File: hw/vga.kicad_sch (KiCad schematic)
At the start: 19 parts, among them J1 Conn_02x05_Odd_Even, J2 DB15_Female_HighDensity_Mount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, U1 74HC4053, U2 23LCV512, U3 ICS501

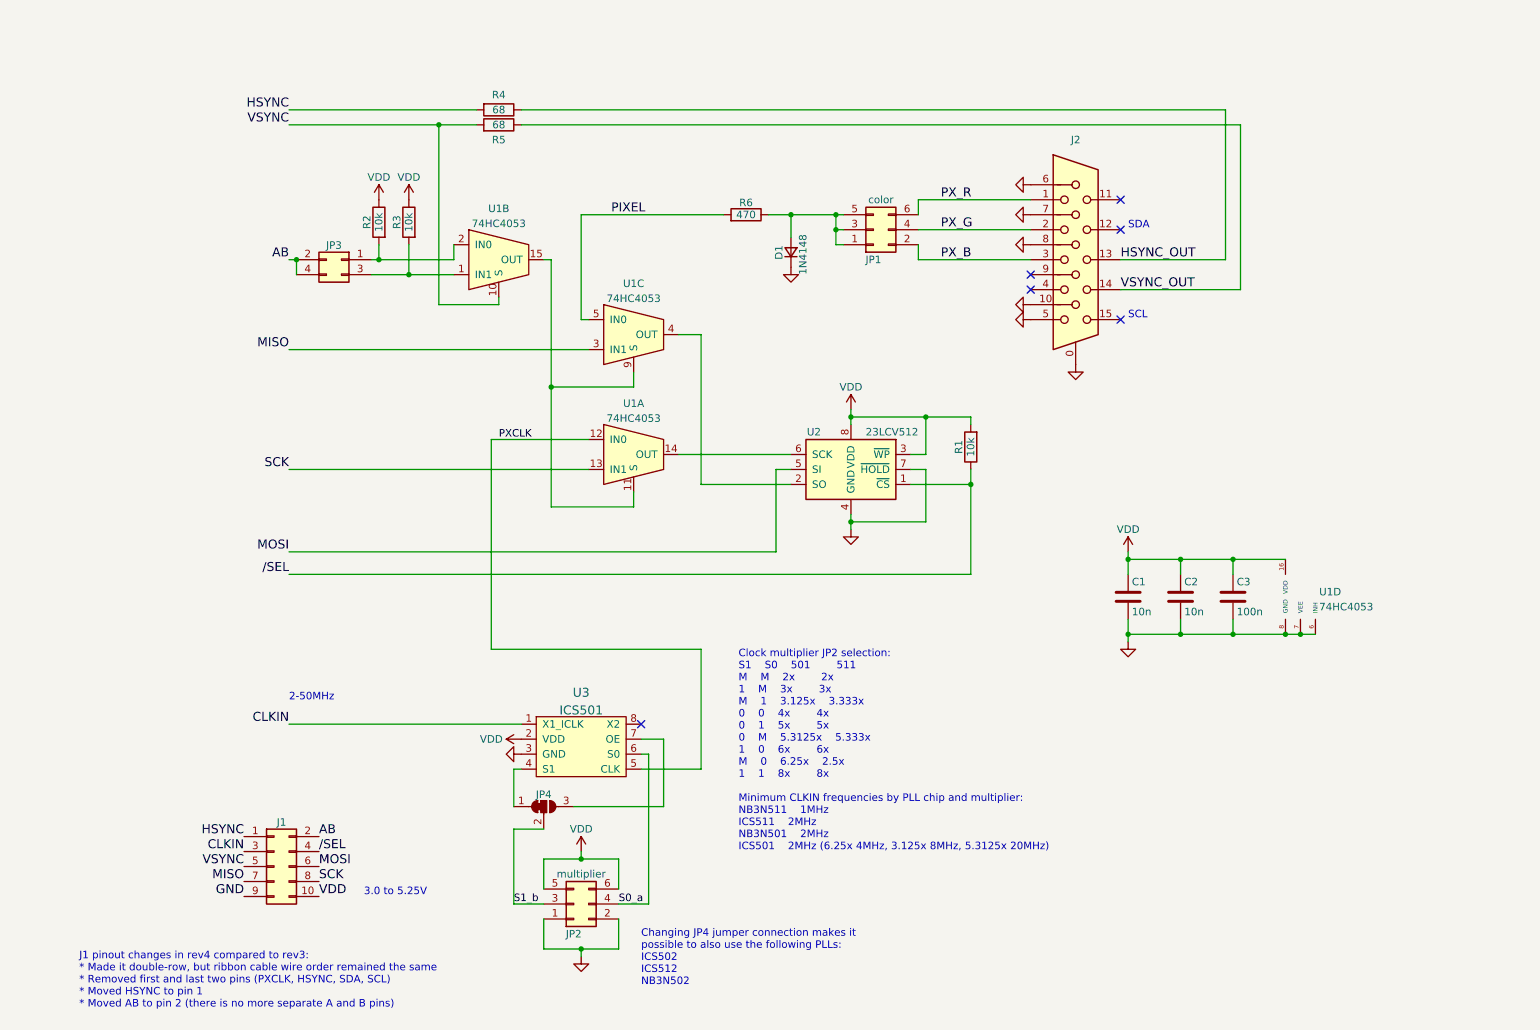
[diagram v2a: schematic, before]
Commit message: Finalized rev4 board. Added post PCB manufacturing TODOs to schematic.
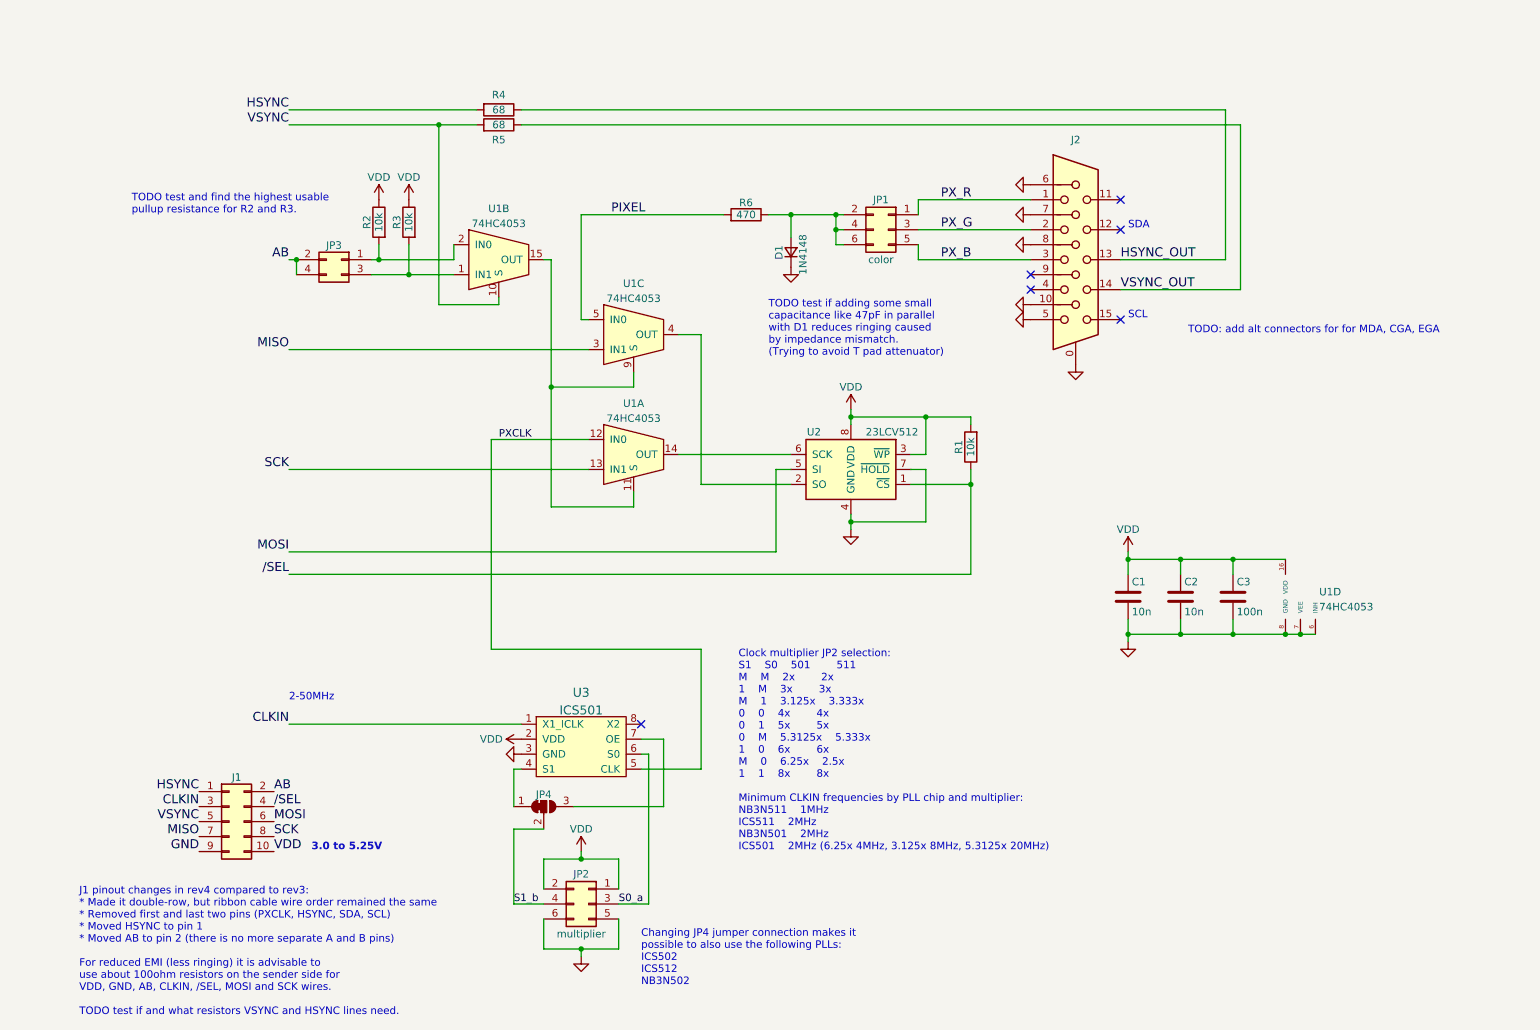
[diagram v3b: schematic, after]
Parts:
- D1: footprint Diode_SMD:D_SOD-323_HandSoldering -> Diode_SMD:D_SOD-123
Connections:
- net GND: now also JP2.5 (Pin_5), JP2.6 (Pin_6); no longer JP2.1 (Pin_1), JP2.2 (Pin_2)
- net PX_B: now also JP1.5 (Pin_5); no longer JP1.2 (Pin_2)
- net PX_G: now also JP1.3 (Pin_3); no longer JP1.4 (Pin_4)
- net PX_R: now also JP1.1 (Pin_1); no longer JP1.6 (Pin_6)
- net S0_a: now also JP2.3 (Pin_3); no longer JP2.4 (Pin_4)
- net S1_b: now also JP2.4 (Pin_4); no longer JP2.3 (Pin_3)
- net VDD: now also JP2.1 (Pin_1), JP2.2 (Pin_2); no longer JP2.5 (Pin_5), JP2.6 (Pin_6)
- new net: D1.2 (A), JP1.2 (Pin_2), JP1.4 (Pin_4), JP1.6 (Pin_6), R6.1
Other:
- note added: "J1 pinout changes in rev4 compared to rev3: * Made it double-row, but ribbon cable wire order remained the same * Removed first and last two pins (PXCLK, HSYNC, SDA, SCL) * Moved HSYNC to pin 1 * Moved AB to pin 2 (there is no more separate A and B pins) For reduced EMI (less ringing) it is advisable to use about 100ohm resistors on the sender side for VDD, GND, AB, CLKIN, /SEL, MOSI and SCK wire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"
- note added: "TODO test and find the highest usable pullup resistance for R2 and R3."
- note added: "TODO test if adding some small capacitance like 47pF in parallel with D1 reduces ringing caused by impedance mismatch. (Trying to avoid T pad attenuator)"
- note added: "TODO: add alt connectors for for MDA, CGA, EGA"
- note removed: "J1 pinout changes in rev4 compared to rev3: * Made it double-row, but ribbon cable wire order remained the same * Removed first and last two pins (PXCLK, HSYNC, SDA, SCL) * Moved HSYNC to pin 1 * Moved AB to pin 2 (there is no more separate A and B pins)"
- moved on the sheet: J1
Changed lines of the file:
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@@
+    (effects (font (size 1.27 1.27)) (justify left bottom))
+  )
+  (text "TODO: add alt connectors for for MDA, CGA, EGA" (at 217.17 76.2 0)
     (effects (font (size 1.27 1.27)) (justify left bottom))
   )
@@
     (effects (font (size 1.27 1.27)) (justify left bottom))
   )
-  (text "J1 pinout changes in rev4 compared to rev3:\n* Made it double-row, but ribbon cable wire order remained the same\n* Removed first and last two pins (PXCLK, HSYNC, SDA, SCL)\n* Moved HSYNC to pin 1\n* Moved AB to pin 2 (there is no more separate A and B pins)"
-    (at 29.21 190.5 0)
-    (effects (font (size 1.27 1.27)) (justify left bottom))
-  )
-  (text "3.0 to 5.25V" (at 77.47 171.45 0)
-    (effects (font (size 1.27 1.27)) (justify left bottom))
+  (text "TODO test if adding some small\ncapacitance like 47pF in parallel\nwith D1 reduces ringing caused\nby impedance mismatch.\n(Trying to avoid T pad attenuator)"
+    (at 146.05 80.01 0)
+    (effects (font (size 1.27 1.27)) (justify left bottom))
+  )
+  (text "J1 pinout changes in rev4 compared to rev3:\n* Made it double-row, but ribbon cable wire order remained the same\n* Removed first and last two pins (PXCLK, HSYNC, SDA, SCL)\n* Moved HSYNC to pin 1\n* Moved AB to pin 2 (there is no more separate A and B pins)\n\nFor reduced EMI (less ringing) it is advisable to\nuse about 100ohm resistors on the sender side for\nVDD, GND, AB, CLKIN, /SEL, MOSI and SCK wires.\n\nTODO test if and what resistors VSYNC and HSYNC lines need."
+    (at 29.21 191.77 0)
+    (effects (font (size 1.27 1.27)) (justify left bottom))
+  )
+  (text "3.0 to 5.25V" (at 68.58 163.83 0)
+    (effects (font (size 1.27 1.27) (thickness 0.254) bold) (justify left bottom))
   )
   (text "SCL" (at 207.01 73.66 0)
@@
     (effects (font (size 1.27 1.27)) (justify left bottom))
   )
-  (label "AB" (at 69.85 161.29 0)
+  (text "TODO test and find the highest usable\npullup resistance for R2 and R3."
+    (at 38.1 55.88 0)
+    (effects (font (size 1.27 1.27)) (justify left bottom))
+  )
+  (label "AB" (at 62.23 153.67 0)
     (effects (font (size 1.524 1.524)) (justify left bottom))
   )
@@
     (effects (font (size 1.27 1.27)) (justify left bottom))
   )
-  (label "VSYNC" (at 57.15 166.37 180)
-    (effects (font (size 1.524 1.524)) (justify right bottom))
-  )
-  (label "/SEL" (at 69.85 163.83 0)
-    (effects (font (size 1.524 1.524)) (justify left bottom))
-  )
-  (label "CLKIN" (at 57.15 163.83 180)
+  (label "VSYNC" (at 49.53 158.75 180)
+    (effects (font (size 1.524 1.524)) (justify right bottom))
+  )
+  (label "/SEL" (at 62.23 156.21 0)
+    (effects (font (size 1.524 1.524)) (justify left bottom))
+  )
+  (label "CLKIN" (at 49.53 156.21 180)
     (effects (font (size 1.524 1.524)) (justify right bottom))
   )
@@
     (effects (font (size 1.524 1.524)) (justify right bottom))
   )
-  (label "SCK" (at 69.85 168.91 0)
+  (label "SCK" (at 62.23 161.29 0)
     (effects (font (size 1.524 1.524)) (justify left bottom))
   )
@@
     (effects (font (size 1.524 1.524)) (justify right bottom))
   )
-  (label "VDD" (at 69.85 171.45 0)
+  (label "VDD" (at 62.23 163.83 0)
     (effects (font (size 1.524 1.524)) (justify left bottom))
   )
@@
     (effects (font (size 1.524 1.524)) (justify left bottom))
   )
-  (label "HSYNC" (at 57.15 161.29 180)
-    (effects (font (size 1.524 1.524)) (justify right bottom))
-  )
-  (label "MISO" (at 57.15 168.91 180)
+  (label "HSYNC" (at 49.53 153.67 180)
+    (effects (font (size 1.524 1.524)) (justify right bottom))
+  )
+  (label "MISO" (at 49.53 161.29 180)
     (effects (font (size 1.524 1.524)) (justify right bottom))
   )
@@
     (effects (font (size 1.524 1.524)) (justify right bottom))
   )
-  (label "MOSI" (at 69.85 166.37 0)
-    (effects (font (size 1.524 1.524)) (justify left bottom))
-  )
-  (label "GND" (at 57.15 171.45 180)
+  (label "MOSI" (at 62.23 158.75 0)
+    (effects (font (size 1.524 1.524)) (justify left bottom))
+  )
+  (label "GND" (at 49.53 163.83 180)
     (effects (font (size 1.524 1.524)) (justify right bottom))
   )
@@
     (pin "1")
   )
-  (symbol (lib_id "Connector_Generic:Conn_02x03_Odd_Even") (at 163.83 58.42 0) (mirror x) (unit 1)
-    (in_bom yes) (on_board yes)
-    (property "Reference" "JP1" (id 0) (at 163.83 63.5 0))
-    (property "Value" "color" (id 1) (at 165.1 53.34 0))
-    (property "Footprint" "Connector_PinHeader_2.54mm:PinHeader_2x03_P2.54mm_Vertical" (id 2) (at 163.83 58.42 0)
-      (effects (font (size 1.27 1.27)) hide)
-    )
-    (property "Datasheet" "https://www.tme.eu/Document/2d4a219a7dd0b1e98a08518b8e9e24c3/67996-XXXXLF.pdf" (id 3) (at 163.83 58.42 0)
-      (effects (font (size 1.27 1.27)) hide)
-    )
-    (property "MFG Name" " Amphenol" (id 4) (at 163.83 58.42 0)
-      (effects (font (size 1.27 1.27)) hide)
-    )
-    (property "MFG Part Num" "67996-206HLF" (id 5) (at 163.83 58.42 0)
-      (effects (font (size 1.27 1.27)) hide)
-    )
-    (property "TME PN" "67996-206HLF" (id 6) (at 163.83 58.42 0)
+  (symbol (lib_id "Connector_Generic:Conn_02x03_Odd_Even") (at 166.37 58.42 0) (mirror y) (unit 1)
+    (in_bom yes) (on_board yes)
+    (property "Reference" "JP1" (id 0) (at 165.1 53.34 0))
+    (property "Value" "color" (id 1) (at 165.1 63.5 0))
+    (property "Footprint" "Connector_PinHeader_2.54mm:PinHeader_2x03_P2.54mm_Vertical" (id 2) (at 166.37 58.42 0)
+      (effects (font (size 1.27 1.27)) hide)
+    )
+    (property "Datasheet" "https://www.tme.eu/Document/2d4a219a7dd0b1e98a08518b8e9e24c3/67996-XXXXLF.pdf" (id 3) (at 166.37 58.42 0)
+      (effects (font (size 1.27 1.27)) hide)
+    )
+    (property "MFG Name" " Amphenol" (id 4) (at 166.37 58.42 0)
+      (effects (font (size 1.27 1.27)) hide)
+    )
+    (property "MFG Part Num" "67996-206HLF" (id 5) (at 166.37 58.42 0)
+      (effects (font (size 1.27 1.27)) hide)
+    )
+    (property "TME PN" "67996-206HLF" (id 6) (at 166.37 58.42 0)
       (effects (font (size 1.27 1.27)) hide)
     )
@@
       (effects (font (size 1.27 1.27)) (justify left))
     )
-    (property "Footprint" "Diode_SMD:D_SOD-323_HandSoldering" (id 2) (at 149.86 62.23 90)
+    (property "Footprint" "Diode_SMD:D_SOD-123" (id 2) (at 149.86 62.23 90)
       (effects (font (size 1.27 1.27)) hide)
     )
@@
     (pin "1")
   )
-  (symbol (lib_id "Connector_Generic:Conn_02x03_Odd_Even") (at 113.03 172.72 0) (mirror x) (unit 1)
-    (in_bom yes) (on_board yes)
-    (property "Reference" "JP2" (id 0) (at 113.03 177.8 0))
-    (property "Value" "multiplier" (id 1) (at 114.3 167.64 0))
-    (property "Footprint" "Connector_PinHeader_2.54mm:PinHeader_2x03_P2.54mm_Vertical" (id 2) (at 113.03 172.72 0)
-      (effects (font (size 1.27 1.27)) hide)
-    )
-    (property "Datasheet" "https://www.tme.eu/Document/2d4a219a7dd0b1e98a08518b8e9e24c3/67996-XXXXLF.pdf" (id 3) (at 113.03 172.72 0)
-      (effects (font (size 1.27 1.27)) hide)
-    )
-    (property "MFG Name" "Amphenol" (id 4) (at 113.03 172.72 0)
-      (effects (font (size 1.27 1.27)) hide)
-    )
-    (property "MFG Part Num" "67996-206HLF" (id 5) (at 113.03 172.72 0)
-      (effects (font (size 1.27 1.27)) hide)
-    )
-    (property "TME PN" "67996-206HLF" (id 6) (at 113.03 172.72 0)
+  (symbol (lib_id "Connector_Generic:Conn_02x03_Odd_Even") (at 115.57 172.72 0) (mirror y) (unit 1)
+    (in_bom yes) (on_board yes)
+    (property "Reference" "JP2" (id 0) (at 114.3 167.64 0))
+    (property "Value" "multiplier" (id 1) (at 114.3 177.8 0))
+    (property "Footprint" "Connector_PinHeader_2.54mm:PinHeader_2x03_P2.54mm_Vertical" (id 2) (at 115.57 172.72 0)
+      (effects (font (size 1.27 1.27)) hide)
+    )
+    (property "Datasheet" "https://www.tme.eu/Document/2d4a219a7dd0b1e98a08518b8e9e24c3/67996-XXXXLF.pdf" (id 3) (at 115.57 172.72 0)
+      (effects (font (size 1.27 1.27)) hide)
+    )
+    (property "MFG Name" "Amphenol" (id 4) (at 115.57 172.72 0)
+      (effects (font (size 1.27 1.27)) hide)
+    )
+    (property "MFG Part Num" "67996-206HLF" (id 5) (at 115.57 172.72 0)
+      (effects (font (size 1.27 1.27)) hide)
+    )
+    (property "TME PN" "67996-206HLF" (id 6) (at 115.57 172.72 0)
       (effects (font (size 1.27 1.27)) hide)
     )
@@
     (pin "8")
   )
-  (symbol (lib_id "Connector_Generic:Conn_02x05_Odd_Even") (at 62.23 166.37 0) (unit 1)
+  (symbol (lib_id "Connector_Generic:Conn_02x05_Odd_Even") (at 54.61 158.75 0) (unit 1)
     (in_bom yes) (on_board yes) (fields_autoplaced)
-    (property "Reference" "J1" (id 0) (at 63.5 158.8572 0))
-    (property "Value" "Conn_02x05_Odd_Even" (id 1) (at 63.5 158.8571 0)
-      (effects (font (size 1.27 1.27)) hide)
-    )
-    (property "Footprint" "Connector_IDC:IDC-Header_2x05_P2.54mm_Vertical" (id 2) (at 62.23 166.37 0)
-      (effects (font (size 1.27 1.27)) hide)
-    )
-    (property "Datasheet" "~" (id 3) (at 62.23 166.37 0)
+    (property "Reference" "J1" (id 0) (at 55.88 151.2372 0))
+    (property "Value" "Conn_02x05_Odd_Even" (id 1) (at 55.88 151.2371 0)
+      (effects (font (size 1.27 1.27)) hide)
+    )
+    (property "Footprint" "Connector_IDC:IDC-Header_2x05_P2.54mm_Vertical" (id 2) (at 54.61 158.75 0)
+      (effects (font (size 1.27 1.27)) hide)
+    )
+    (property "Datasheet" "~" (id 3) (at 54.61 158.75 0)
       (effects (font (size 1.27 1.27)) hide)
     )
@@
     )
     (path "/00000000-0000-0000-0000-000058f240a6"
-      (reference "D1") (unit 1) (value "1N4148") (footprint "Diode_SMD:D_SOD-323_HandSoldering")
+      (reference "D1") (unit 1) (value "1N4148") (footprint "Diode_SMD:D_SOD-123")
     )
     (path "/ada82fe7-ccfa-46c7-b351-2c5340a35c0b"

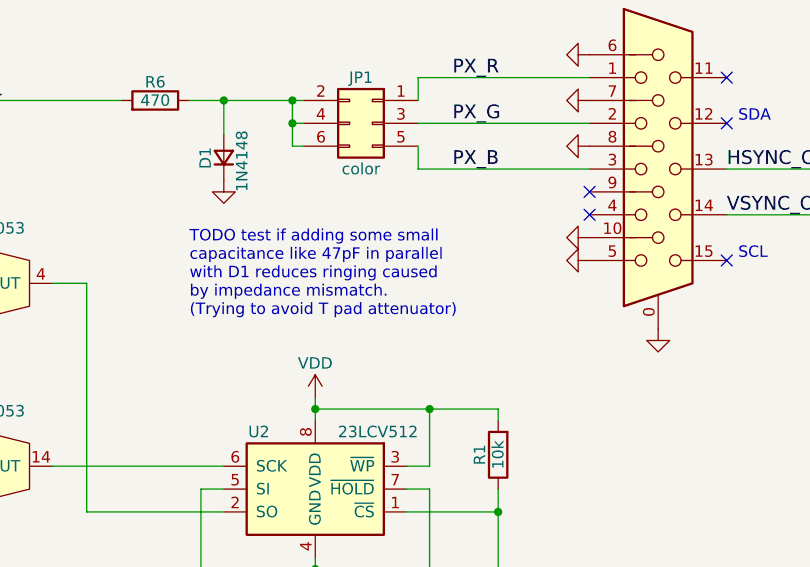
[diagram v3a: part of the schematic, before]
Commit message: Updated folder structure
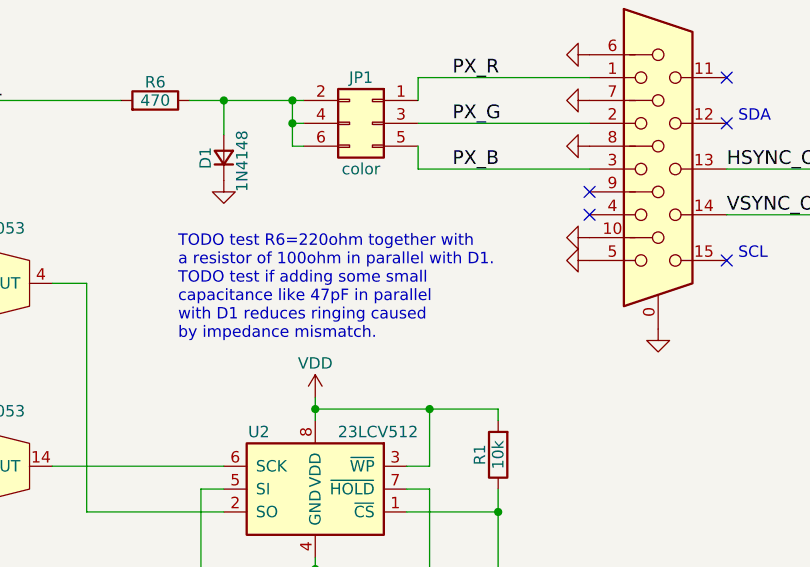
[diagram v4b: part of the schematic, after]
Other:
- note added: "TODO test R6=220ohm together with a resistor of 100ohm in parallel with D1. TODO test if adding some small capacitance like 47pF in parallel with D1 reduces ringing caused by impedance mismatch."
- note removed: "TODO test if adding some small capacitance like 47pF in parallel with D1 reduces ringing caused by impedance mismatch. (Trying to avoid T pad attenuator)"
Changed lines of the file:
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@@
     (effects (font (size 1.27 1.27)) (justify left bottom))
   )
-  (text "TODO test if adding some small\ncapacitance like 47pF in parallel\nwith D1 reduces ringing caused\nby impedance mismatch.\n(Trying to avoid T pad attenuator)"
-    (at 146.05 80.01 0)
+  (text "TODO test R6=220ohm together with\na resistor of 100ohm in parallel with D1.\nTODO test if adding some small\ncapacitance like 47pF in parallel\nwith D1 reduces ringing caused\nby impedance mismatch."
+    (at 144.78 82.55 0)
     (effects (font (size 1.27 1.27)) (justify left bottom))
   )
